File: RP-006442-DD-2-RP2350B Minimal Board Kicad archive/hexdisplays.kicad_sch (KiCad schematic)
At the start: 2 parts, among them U8 HT16K33A-24SSOP, U9 CC56-12EWA

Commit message: Big update
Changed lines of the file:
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@@
 		)
-	)
-	(junction
-		(at 113.03 99.06)
-		(diameter 0)
-		(color 0 0 0 0)
-	)
-	(junction
-		(at 102.87 96.52)
-		(diameter 0)
-		(color 0 0 0 0)
 	)
 	(no_connect
@@
 	(wire
 		(pts
-			(xy 102.87 96.52) (xy 106.68 96.52)
-		)
-		(stroke
-			(width 0)
-			(type default)
-		)
-	)
-	(wire
-		(pts
 			(xy 93.98 85.09) (xy 93.98 93.98)
 		)
@@
 	(wire
 		(pts
-			(xy 93.98 96.52) (xy 102.87 96.52)
+			(xy 93.98 96.52) (xy 106.68 96.52)
 		)
 		(stroke
@@
 	(wire
 		(pts
-			(xy 93.98 99.06) (xy 113.03 99.06)
+			(xy 93.98 99.06) (xy 106.68 99.06)
 		)
 		(stroke
@@
 	(wire
 		(pts
-			(xy 102.87 93.98) (xy 102.87 96.52)
-		)
-		(stroke
-			(width 0)
-			(type default)
-		)
-	)
-	(wire
-		(pts
-			(xy 116.84 99.06) (xy 113.03 99.06)
-		)
-		(stroke
-			(width 0)
-			(type default)
-		)
-	)
-	(wire
-		(pts
 			(xy 93.98 111.76) (xy 104.14 111.76)
 		)
@@
 		(pts
 			(xy 256.54 115.57) (xy 247.65 115.57)
-		)
-		(stroke
-			(width 0)
-			(type default)
-		)
-	)
-	(wire
-		(pts
-			(xy 113.03 99.06) (xy 113.03 93.98)
 		)
 		(stroke
@@
 	(hierarchical_label "SCL"
 		(shape input)
-		(at 116.84 99.06 0)
-		(effects
-			(font
+		(at 106.68 99.06 0)
+		(effects
+			(font

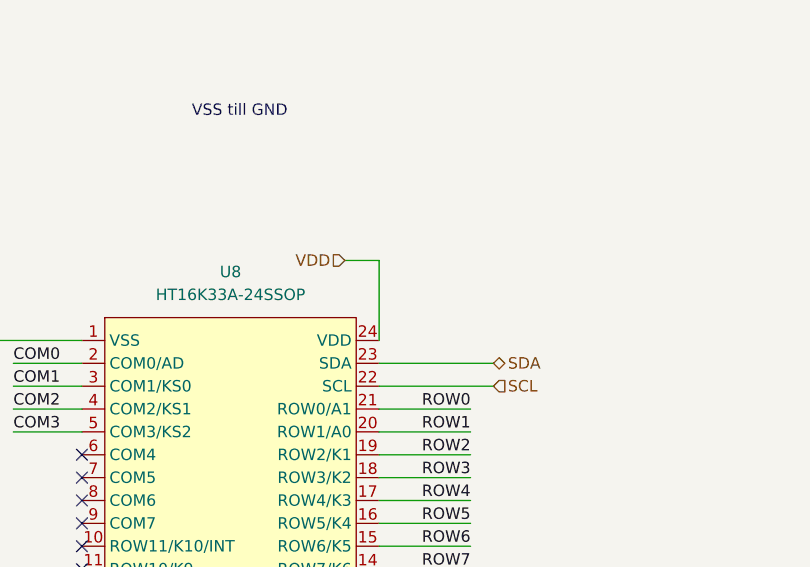
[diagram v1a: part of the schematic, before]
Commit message: Added capacitor to LED driver power input
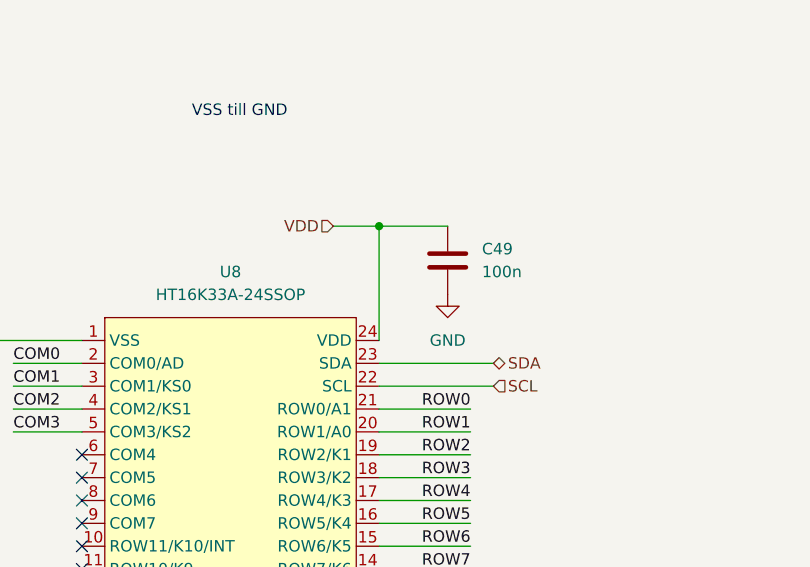
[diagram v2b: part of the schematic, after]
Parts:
- added C49: 100n, Capacitor_SMD:C_0402_1005Metric, symbol Device:C
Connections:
- net GND: now also C49.2
- net VDD: now also C49.1
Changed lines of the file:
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@@
 		)
+	)
+	(junction
+		(at 93.98 81.28)
+		(diameter 0)
+		(color 0 0 0 0)
 	)
 	(no_connect
@@
 	(wire
 		(pts
-			(xy 93.98 85.09) (xy 93.98 93.98)
+			(xy 93.98 81.28) (xy 93.98 93.98)
 		)
 		(stroke
@@
 	(wire
 		(pts
-			(xy 90.17 85.09) (xy 93.98 85.09)
+			(xy 88.9 81.28) (xy 93.98 81.28)
 		)
 		(stroke
@@
 		(pts
 			(xy 93.98 119.38) (xy 104.14 119.38)
+		)
+		(stroke
+			(width 0)
+			(type default)
+		)
+	)
+	(wire
+		(pts
+			(xy 93.98 81.28) (xy 101.6 81.28)
 		)
 		(stroke
@@
 	(hierarchical_label "VDD"
 		(shape input)
-		(at 90.17 85.09 180)
+		(at 88.9 81.28 180)
 		(effects
 			(font
@@
 			)
 			(justify right)
+		)
+	)
+	(symbol
+		(lib_id "power:GND")
+		(at 101.6 88.9 0)
+		(unit 1)
+		(exclude_from_sim no)
+		(in_bom yes)
+		(on_board yes)
+		(dnp no)
+		(fields_autoplaced yes)
+		(property "Reference" "#PWR081"
+			(at 101.6 95.25 0)
+			(effects
+				(font
+					(size 1.27 1.27)
+				)
+				(hide yes)
+			)
+		)
+		(property "Value" "GND"
+			(at 101.6 93.98 0)
+			(effects
+				(font
+					(size 1.27 1.27)
+				)
+			)
+		)
+		(property "Footprint" ""
+			(at 101.6 88.9 0)
+			(effects
+				(font
+					(size 1.27 1.27)
+				)
+				(hide yes)
+			)
+		)
+		(property "Datasheet" ""
+			(at 101.6 88.9 0)
+			(effects
+				(font
+					(size 1.27 1.27)
+				)
+				(hide yes)
+			)
+		)
+		(property "Description" "Power symbol creates a global label with name \"GND\" , ground"
+			(at 101.6 88.9 0)
+			(effects
+				(font
+					(size 1.27 1.27)
+				)
+				(hide yes)
+			)
+		)
+		(pin "1"
+		)
+		(instances
+			(project ""
+				(path "/94683f5c-9cd9-448e-be96-9792537b5cb8/09473c75-4602-45fc-a2db-44d591bf96bf"
+					(reference "#PWR081")
+					(unit 1)
+				)
+			)
 		)
 	)
@@
 					(unit 1)
 				)
+			)
+		)
+	)
+	(symbol
+		(lib_id "Device:C")
+		(at 101.6 85.09 0)
+		(unit 1)
+		(exclude_from_sim no)
+		(in_bom yes)
+		(on_board yes)
+		(dnp no)
+		(fields_autoplaced yes)
+		(property "Reference" "C49"
+			(at 105.41 83.8199 0)
+			(effects
+				(font
+					(size 1.27 1.27)
+				)
+				(justify left)
+			)
+		)
+		(property "Value" "100n"
+			(at 105.41 86.3599 0)
+			(effects
+				(font
+					(size 1.27 1.27)
+				)
+				(justify left)
+			)
+		)
+		(property "Footprint" "Capacitor_SMD:C_0402_1005Metric"
+			(at 102.5652 88.9 0)
+			(effects
+				(font
+					(size 1.27 1.27)
+				)
+				(hide yes)
+			)
+		)
+		(property "Datasheet" "~"
+			(at 101.6 85.09 0)
+			(effects
+				(font
+					(size 1.27 1.27)
+				)
+				(hide yes)
+			)
+		)
+		(property "Description" "Unpolarized capacitor"
+			(at 101.6 85.09 0)
+			(effects
+				(font
+					(size 1.27 1.27)
+				)
+				(hide yes)
+			)
+		)
+		(pin "2"
+		)
+		(pin "1"
+		)
+		(instances
+			(project ""
+				(path "/94683f5c-9cd9-448e-be96-9792537b5cb8/09473c75-4602-45fc-a2db-44d591bf96bf"
+					(reference "C49")
+					(unit 1)
+				)

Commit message: PNG and LCSC numbers
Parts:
- C49: LCSC (none) -> C1525
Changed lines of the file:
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@@
+			)
+		)
+		(property "LCSC" "C1525"
+			(at 101.6 85.09 0)
+			(effects
+				(font
+					(size 1.27 1.27)
+				)
+				(hide yes)
 			)
 		)

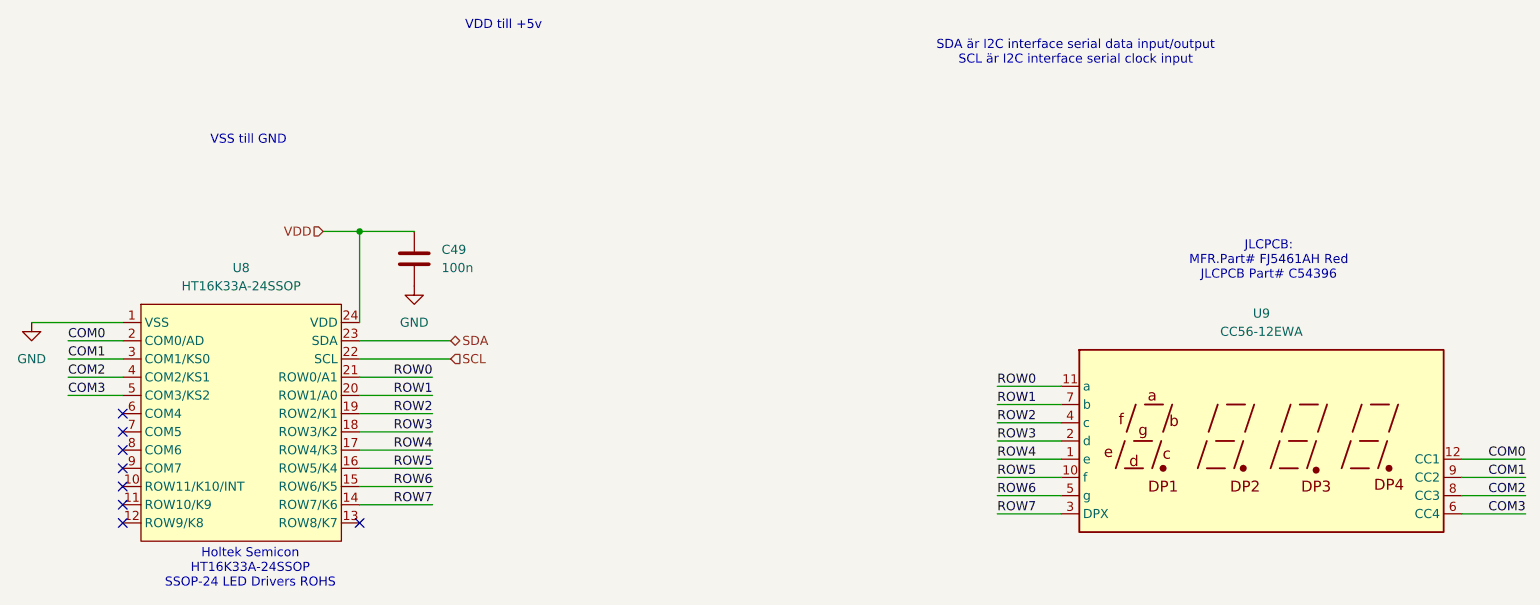
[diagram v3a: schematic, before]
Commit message: Added LCSC numbers to parts
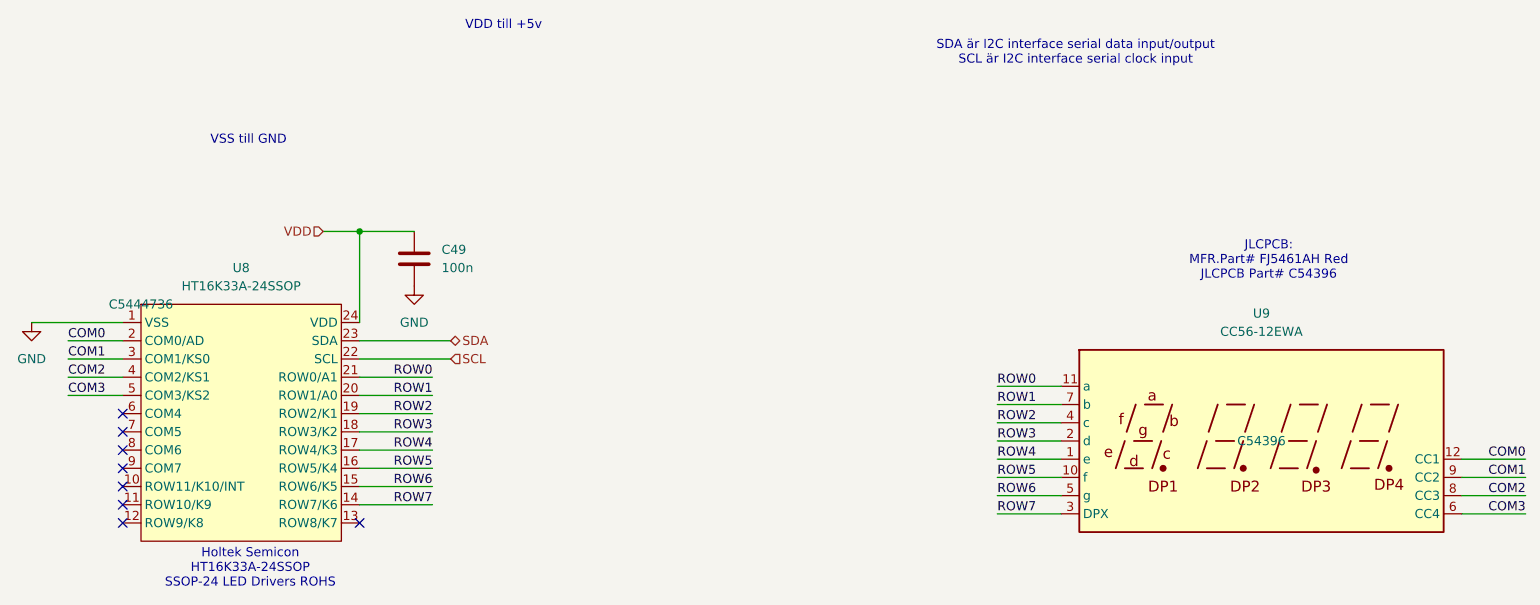
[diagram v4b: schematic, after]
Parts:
- U8: LCSC (none) -> C5444736
- U9: LCSC (none) -> C54396
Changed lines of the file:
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@@
+			)
+		)
+		(property "LCSC" "C54396"
+			(at 219.71 110.49 0)
+			(effects
+				(font
+					(size 1.27 1.27)
+				)
 			)
 		)
@@
 			)
 		)
+		(property "LCSC" "C5444736"
+			(at 63.5 91.44 0)
+			(effects
+				(font
+					(size 1.27 1.27)
+				)
+			)
+		)
